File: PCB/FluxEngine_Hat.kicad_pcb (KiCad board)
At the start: 2 copper layers, 83.3 x 24.1 mm, 4 parts, among them J1 CY8CKIT-059 usb & button face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, J2 Conn_02x05_Odd_Even, P1 FDD_IBMPC_host, P2 FDD_SA800_host

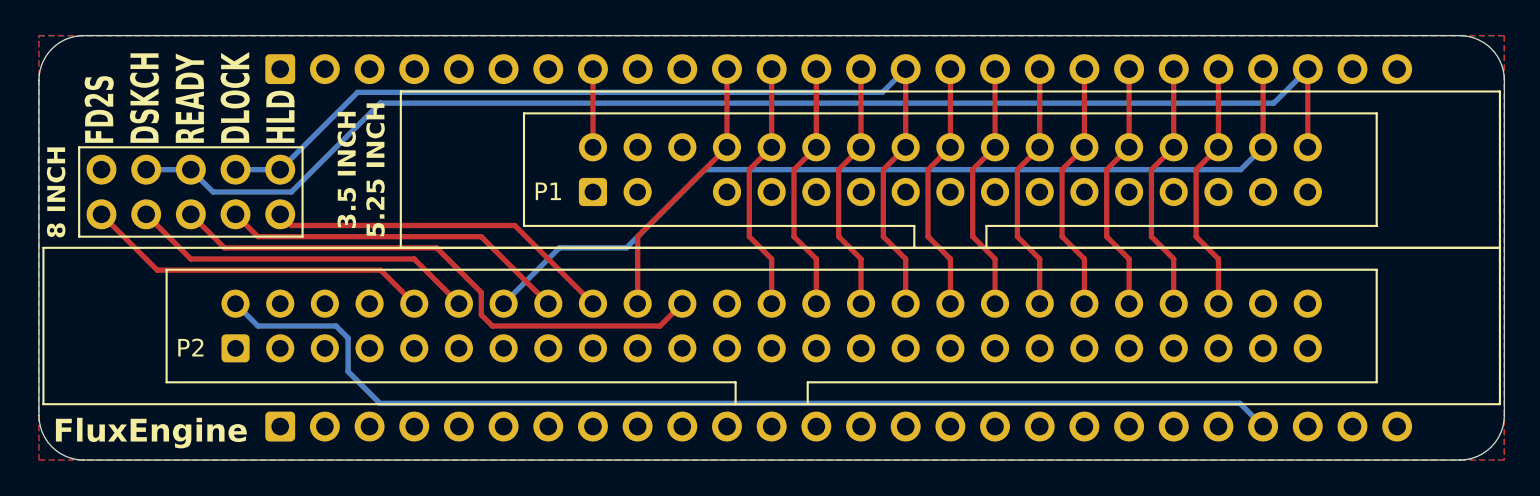
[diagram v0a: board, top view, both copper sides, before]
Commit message: better jumper arrangement, fix some signal names
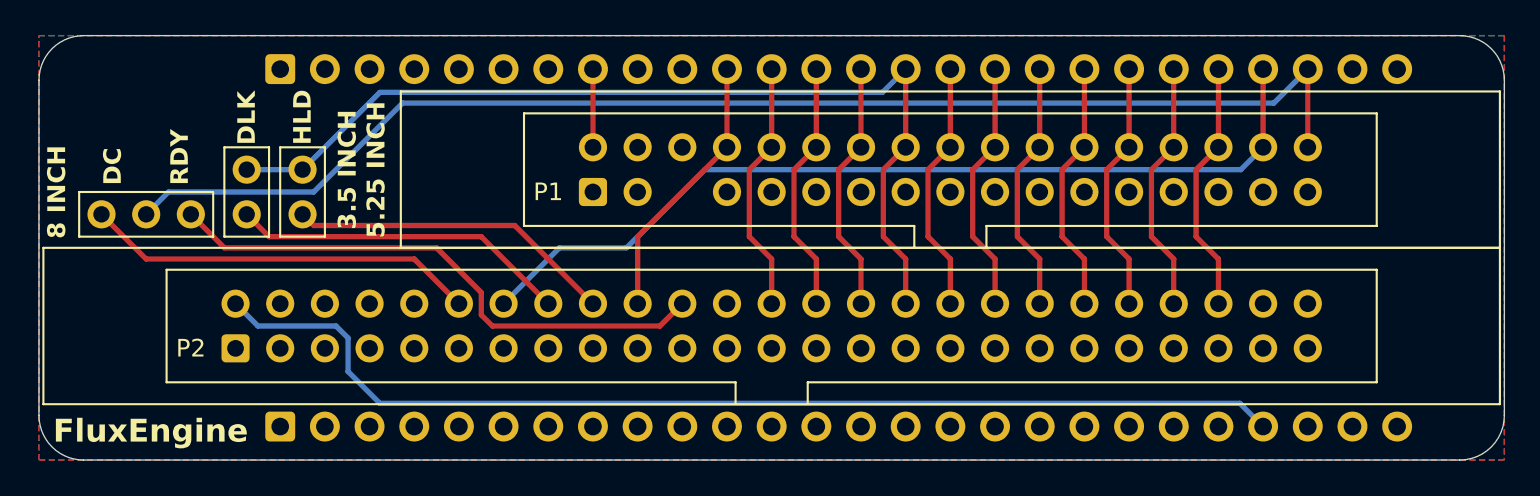
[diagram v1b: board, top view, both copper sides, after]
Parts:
- removed J2: Conn_02x05_Odd_Even, 000_LOCAL:PinHeader_2x05_P2.54mm_Vertical
- added JP1: Jumper_3_Bridged12, 000_LOCAL:PinHeader_1x03_P2.54mm_Vertical, F.Cu at (106.0, 94.6)
- added JP2: Jumper_2_Open, 000_LOCAL:PinHeader_1x02_P2.54mm_Vertical, F.Cu at (114.3, 94.6)
- added JP3: Jumper_2_Open, 000_LOCAL:PinHeader_1x02_P2.54mm_Vertical, F.Cu at (117.5, 94.6)
- J1: value CY8CKIT-059 usb & button face away from hat -> CY8CKIT-059
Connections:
- net /RDATA renamed /~{RDATA}
- net /TG43 renamed /~{TG43}
- net /WDATA renamed /~{WDATA}
- net /~{READY} renamed /~{DSKCHG}
- J1 pad J1_10: /RX -> unconnected-(J1-12.6-PadJ1_10)
- J1 pad J1_9: /TX -> unconnected-(J1-12.7-PadJ1_9)
- J1 pad J2_24: /INDEX360 -> unconnected-(J1-3.1-PadJ2_24)
- J1 pad J2_25: /INDEX300 -> unconnected-(J1-3.0-PadJ2_25)
- P2 pad 10: /~{FD2S} -> unconnected-(P2-~{FD2S}-Pad10)
- P2 pad 12: /DC -> /~{DC}
- P2 pad 16: /~{INUSE} -> /~{DLOCK}
- P2 pad 18: /~{HLOAD} -> /~{HLD}
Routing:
- net /~{DC}: track 0.00 -> 22.4 mm
- net /~{HLOAD}: track 19.9 -> 0.00 mm
- net /DC: track 19.9 -> 0.00 mm
- net /~{FD2S}: track 19.9 -> 0.00 mm
- net /~{INUSE}: track 19.9 -> 0.00 mm
- net /~{DLOCK}: track 0.00 -> 19.2 mm
- net /~{HLD}: track 0.00 -> 18.6 mm
- net /~{SEL4}: track 54.9 -> 54.2 mm
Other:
- board text added: "DC"
- board text added: "DLK"
- board text added: "HLD"
- board text added: "RDY"
- board text removed: "FD2S DSKCH READY DLOCK HLD"

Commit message: silkscreen & pics
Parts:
- J1: value CY8CKIT-059 -> CY8CKIT-059 usb & button face away from hat
